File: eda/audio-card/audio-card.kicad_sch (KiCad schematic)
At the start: 1 part, among them J1 AudioJack2_SwitchT

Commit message: Interim commit
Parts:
- removed J1: AudioJack2_SwitchT, Connector_Audio:Jack_3.5mm_PJ320E_Horizontal, symbol Connector_Audio:AudioJack2_SwitchT
- added U1: 74LS74, symbol 74ls593:74LS74
- added U3: 74HCT138, Package_DIP:DIP-16_W10.16mm, symbol 74ls593:74LS138
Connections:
- new net A0: U3.3 (A2)
- new net A1: U3.2 (A1)
- new net A2: U3.1 (A0)
- new net Channel/~{NoteLatch}: U3.14 (O1)
- new net Channel/~{OctaveLatch}: U3.15 (O0)
- new net Channel/~{VolumeLatch}: U3.13 (O2)
- new net Expansion/Clock: U3.6 (E3)
- new net Expansion/R~{W}: U3.4 (E1)
- new net Expansion/~{CS}: U3.5 (E2)
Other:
- added sheet Output stage (output.kicad_sch)
- sheet Channel ports: added D[0..7], MainClock, SoundOut, ~{NoteLatch}, ~{OctaveLatch}, ~{Reset}, ~{VolumeLatch}; removed none
- sheet Expansion ports: added A[0..15], Clock, D[0..7], GND, R~{W}, VCC, ~{CS}, ~{IRQ}, ~{RST}; removed none
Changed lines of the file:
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@@
 (kicad_sch (version 20230121) (generator eeschema)
   (paper "A4")
-  (symbol (lib_id "Connector_Audio:AudioJack2_SwitchT") (at 219.075 62.23 0) (unit 1)
+  (bus_entry (at 64.77 69.215) (size 2.54 2.54)
+    (stroke (width 0) (type default))
+  )
+  (bus_entry (at 64.77 74.295) (size 2.54 2.54)
+    (stroke (width 0) (type default))
+  )
+  (bus_entry (at 64.77 71.755) (size 2.54 2.54)
+    (stroke (width 0) (type default))
+  )
+  (wire (pts (xy 67.31 74.295) (xy 73.025 74.295))
+    (stroke (width 0) (type default))
+  )
+  (bus (pts (xy 111.76 45.085) (xy 76.2 45.085))
+    (stroke (width 0) (type default))
+  )
+  (wire (pts (xy 60.96 84.455) (xy 73.025 84.455))
+    (stroke (width 0) (type default))
+  )
+  (wire (pts (xy 111.76 50.8) (xy 100.965 50.8))
+    (stroke (width 0) (type default))
+  )
+  (bus (pts (xy 60.96 81.915) (xy 64.77 81.915))
+    (stroke (width 0) (type default))
+  )
+  (wire (pts (xy 74.295 50.165) (xy 74.295 42.545))
+    (stroke (width 0) (type default))
+  )
+  (bus (pts (xy 76.2 45.085) (xy 76.2 52.07))
+    (stroke (width 0) (type default))
+  )
+  (wire (pts (xy 104.775 76.835) (xy 98.425 76.835))
+    (stroke (width 0) (type default))
+  )
+  (wire (pts (xy 60.96 86.995) (xy 73.025 86.995))
+    (stroke (width 0) (type default))
+  )
+  (wire (pts (xy 67.31 71.755) (xy 73.025 71.755))
+    (stroke (width 0) (type default))
+  )
+  (wire (pts (xy 60.96 50.165) (xy 74.295 50.165))
+    (stroke (width 0) (type default))
+  )
+  (wire (pts (xy 104.775 54.61) (xy 104.775 76.835))
+    (stroke (width 0) (type default))
+  )
+  (bus (pts (xy 60.96 52.07) (xy 76.2 52.07))
+    (stroke (width 0) (type default))
+  )
+  (bus (pts (xy 64.77 71.755) (xy 64.77 74.295))
+    (stroke (width 0) (type default))
+  )
+  (wire (pts (xy 67.31 76.835) (xy 73.025 76.835))
+    (stroke (width 0) (type default))
+  )
+  (wire (pts (xy 102.87 74.295) (xy 102.87 52.705))
+    (stroke (width 0) (type default))
+  )
+  (wire (pts (xy 102.87 52.705) (xy 111.76 52.705))
+    (stroke (width 0) (type default))
+  )
+  (wire (pts (xy 100.965 50.8) (xy 100.965 71.755))
+    (stroke (width 0) (type default))
+  )
+  (bus (pts (xy 64.77 69.215) (xy 64.77 71.755))
+    (stroke (width 0) (type default))
+  )
+  (wire (pts (xy 60.96 89.535) (xy 73.025 89.535))
+    (stroke (width 0) (type default))
+  )
+  (wire (pts (xy 100.965 71.755) (xy 98.425 71.755))
+    (stroke (width 0) (type default))
+  )
+  (bus (pts (xy 64.77 74.295) (xy 64.77 81.915))
+    (stroke (width 0) (type default))
+  )
+  (wire (pts (xy 98.425 74.295) (xy 102.87 74.295))
+    (stroke (width 0) (type default))
+  )
+  (wire (pts (xy 111.76 54.61) (xy 104.775 54.61))
+    (stroke (width 0) (type default))
+  )
+  (wire (pts (xy 74.295 42.545) (xy 111.76 42.545))
+    (stroke (width 0) (type default))
+  )
+  (label "A2" (at 70.485 71.755 0)
+    (effects (font (size 1.27 1.27)) (justify left bottom))
+  )
+  (label "A0" (at 70.485 76.835 0)
+    (effects (font (size 1.27 1.27)) (justify left bottom))
+  )
+  (label "A1" (at 70.485 74.295 0)
+    (effects (font (size 1.27 1.27)) (justify left bottom))
+  )
+  (symbol (lib_id "74ls593:74LS74") (at 42.545 182.245 0) (unit 3)
     (in_bom yes) (on_board yes) (dnp no) (fields_autoplaced)
-    (property "Reference" "J1" (at 218.44 54.61 0)
-      (effects (font (size 1.27 1.27)))
-    )
-    (property "Value" "AudioJack2_SwitchT" (at 218.44 57.15 0)
-      (effects (font (size 1.27 1.27)))
-    )
-    (property "Footprint" "Connector_Audio:Jack_3.5mm_PJ320E_Horizontal" (at 219.075 62.23 0)
-      (effects (font (size 1.27 1.27)) hide)
-    )
-    (property "Datasheet" "~" (at 219.075 62.23 0)
-      (effects (font (size 1.27 1.27)) hide)
-    )
-    (pin "S")
-    (pin "T")
-    (pin "TN")
+    (property "Reference" "U1" (at 49.53 181.61 0)
+      (effects (font (size 1.27 1.27)) (justify left))
+    )
+    (property "Value" "74LS74" (at 49.53 184.15 0)
+      (effects (font (size 1.27 1.27)) (justify left))
+    )
+    (property "Footprint" "" (at 42.545 182.245 0)
+      (effects (font (size 1.27 1.27)) hide)
+    )
+    (property "Datasheet" "74xx/74hc_hct74.pdf" (at 42.545 182.245 0)
+      (effects (font (size 1.27 1.27)) hide)
+    )
+    (pin "1")
+    (pin "2")
+    (pin "3")
+    (pin "4")
+    (pin "5")
+    (pin "6")
+    (pin "10")
+    (pin "11")
+    (pin "12")
+    (pin "13")
+    (pin "8")
+    (pin "9")
+    (pin "14")
+    (pin "7")
     (instances
       (project "audio-card"
         (path "/b2d5e230-38ae-42d2-af04-44d0ea9b43d4"
-          (reference "J1") (unit 1)
+          (reference "U1") (unit 3)
+        )
+      )
+    )
+  )
+  (symbol (lib_id "74ls593:74LS138") (at 85.725 79.375 0) (unit 1)
+    (in_bom yes) (on_board yes) (dnp no) (fields_autoplaced)
+    (property "Reference" "U3" (at 87.6809 65.405 0)
+      (effects (font (size 1.27 1.27)) (justify left))
+    )
+    (property "Value" "74HCT138" (at 87.6809 67.945 0)
+      (effects (font (size 1.27 1.27)) (justify left))
+    )
+    (property "Footprint" "Package_DIP:DIP-16_W10.16mm" (at 85.725 79.375 0)
+      (effects (font (size 1.27 1.27)) hide)
+    )
+    (property "Datasheet" "http://www.ti.com/lit/gpn/sn74LS138" (at 85.725 79.375 0)
+      (effects (font (size 1.27 1.27)) hide)
+    )
+    (pin "1")
+    (pin "10")
+    (pin "11")
+    (pin "12")
+    (pin "13")
+    (pin "14")
+    (pin "15")
+    (pin "16")
+    (pin "2")
+    (pin "3")
+    (pin "4")
+    (pin "5")
+    (pin "6")
+    (pin "7")
+    (pin "8")
+    (pin "9")
+    (instances
+      (project "audio-card"
+        (path "/b2d5e230-38ae-42d2-af04-44d0ea9b43d4"
+          (reference "U3") (unit 1)
         )
       )
@@
       (effects (font (size 1.27 1.27)) (justify left top))
     )
+    (pin "D[0..7]" tri_state (at 60.96 52.07 0)
+      (effects (font (size 1.27 1.27)) (justify right))
+    )
+    (pin "GND" output (at 46.355 90.17 180)
+      (effects (font (size 1.27 1.27)) (justify left))
+    )
+    (pin "R~{W}" output (at 60.96 89.535 0)
+      (effects (font (size 1.27 1.27)) (justify right))
+    )
+    (pin "Clock" output (at 60.96 84.455 0)
+      (effects (font (size 1.27 1.27)) (justify right))
+    )
+    (pin "~{CS}" output (at 60.96 86.995 0)
+      (effects (font (size 1.27 1.27)) (justify right))
+    )
+    (pin "~{IRQ}" output (at 60.96 60.96 0)
+      (effects (font (size 1.27 1.27)) (justify right))
+    )
+    (pin "~{RST}" bidirectional (at 60.96 50.165 0)
+      (effects (font (size 1.27 1.27)) (justify right))
+    )
+    (pin "VCC" output (at 46.355 48.895 180)
+      (effects (font (size 1.27 1.27)) (justify left))
+    )
+    (pin "A[0..15]" output (at 60.96 81.915 0)
+      (effects (font (size 1.27 1.27)) (justify right))
+    )
     (instances
       (project "audio-card"
@@
     )
   )
-  (sheet (at 113.03 34.29) (size 16.51 25.4) (fields_autoplaced)
+  (sheet (at 173.99 83.82) (size 12.7 3.81) (fields_autoplaced)
     (stroke (width 0.1524) (type solid))
     (fill (color 0 0 0 0.0000))
-    (property "Sheetname" "Channel" (at 113.03 33.5784 0)
+    (property "Sheetname" "Output stage" (at 173.99 83.1084 0)
       (effects (font (size 1.27 1.27)) (justify left bottom))
     )
-    (property "Sheetfile" "channel.kicad_sch" (at 113.03 60.2746 0)
+    (property "Sheetfile" "output.kicad_sch" (at 173.99 88.2146 0)
       (effects (font (size 1.27 1.27)) (justify left top))
     )
-    (instances
+    (pin "SoundIn" input (at 173.99 85.725 180)
+      (effects (font (size 1.27 1.27)) (justify left))
+    )
+    (instances
+      (project "audio-card"
+        (path "/b2d5e230-38ae-42d2-af04-44d0ea9b43d4" (page "4"))
+      )
+    )
+  )
+  (sheet (at 111.76 37.465) (size 16.51 25.4) (fields_autoplaced)
+    (stroke (width 0.1524) (type solid))
+    (fill (color 0 0 0 0.0000))
+    (property "Sheetname" "Channel" (at 111.76 36.7534 0)
+      (effects (font (size 1.27 1.27)) (justify left bottom))
+    )
+    (property "Sheetfile" "channel.kicad_sch" (at 111.76 63.4496 0)
+      (effects (font (size 1.27 1.27)) (justify left top))
+    )
+    (pin "~{Reset}" input (at 111.76 42.545 180)
+      (effects (font (size 1.27 1.27)) (justify left))
+    )
+    (pin "~{NoteLatch}" input (at 111.76 52.705 180)
+      (effects (font (size 1.27 1.27)) (justify left))
+    )
+    (pin "MainClock" input (at 111.76 39.37 180)
+      (effects (font (size 1.27 1.27)) (justify left))
+    )
+    (pin "SoundOut" output (at 128.27 60.325 0)
+      (effects (font (size 1.27 1.27)) (justify right))
+    )
+    (pin "D[0..7]" input (at 111.76 45.085 180)
+      (effects (font (size 1.27 1.27)) (justify left))
+    )
+    (pin "~{OctaveLatch}" input (at 111.76 50.8 180)
+      (effects (font (size 1.27 1.27)) (justify left))
+    )
+    (pin "~{VolumeLatch}" input (at 111.76 54.61 180)
+      (effects (font (size 1.27 1.27)) (justify left))
+    )
+    (instances

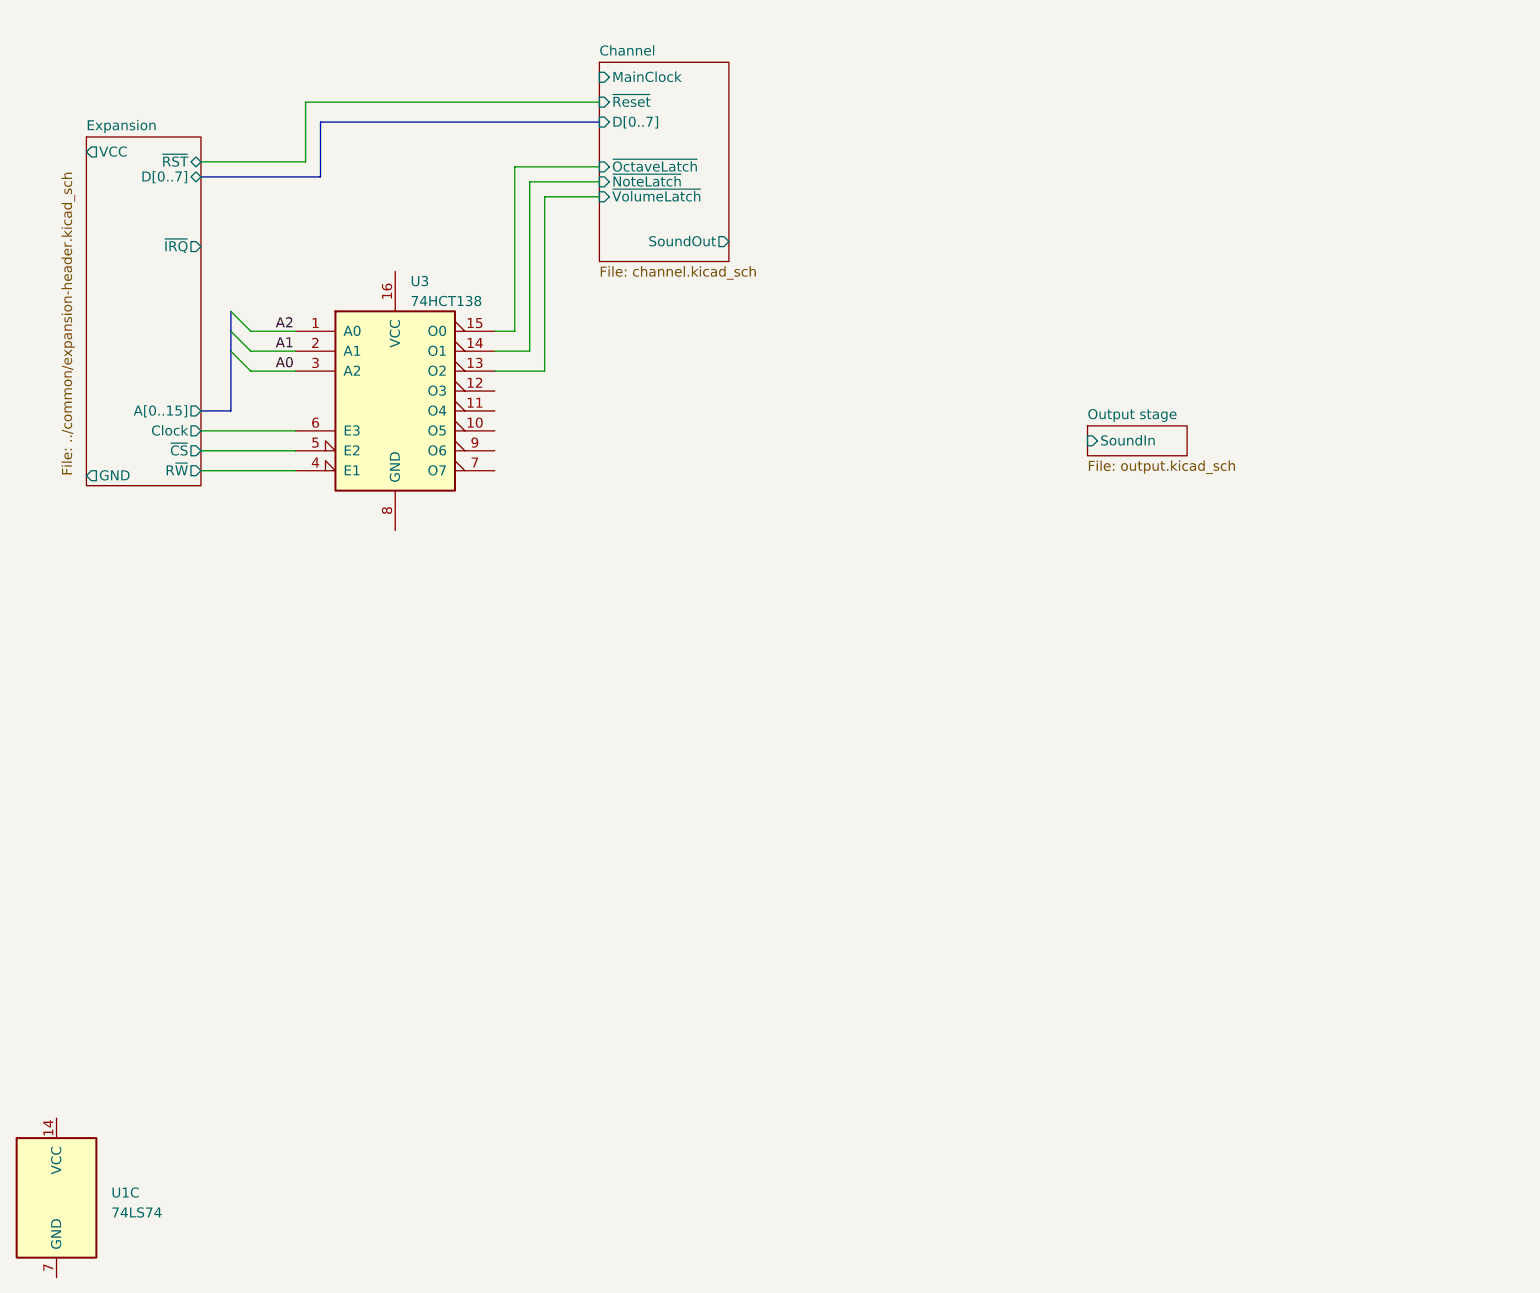
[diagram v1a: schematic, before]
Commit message: Start converting audio card to analog synth base
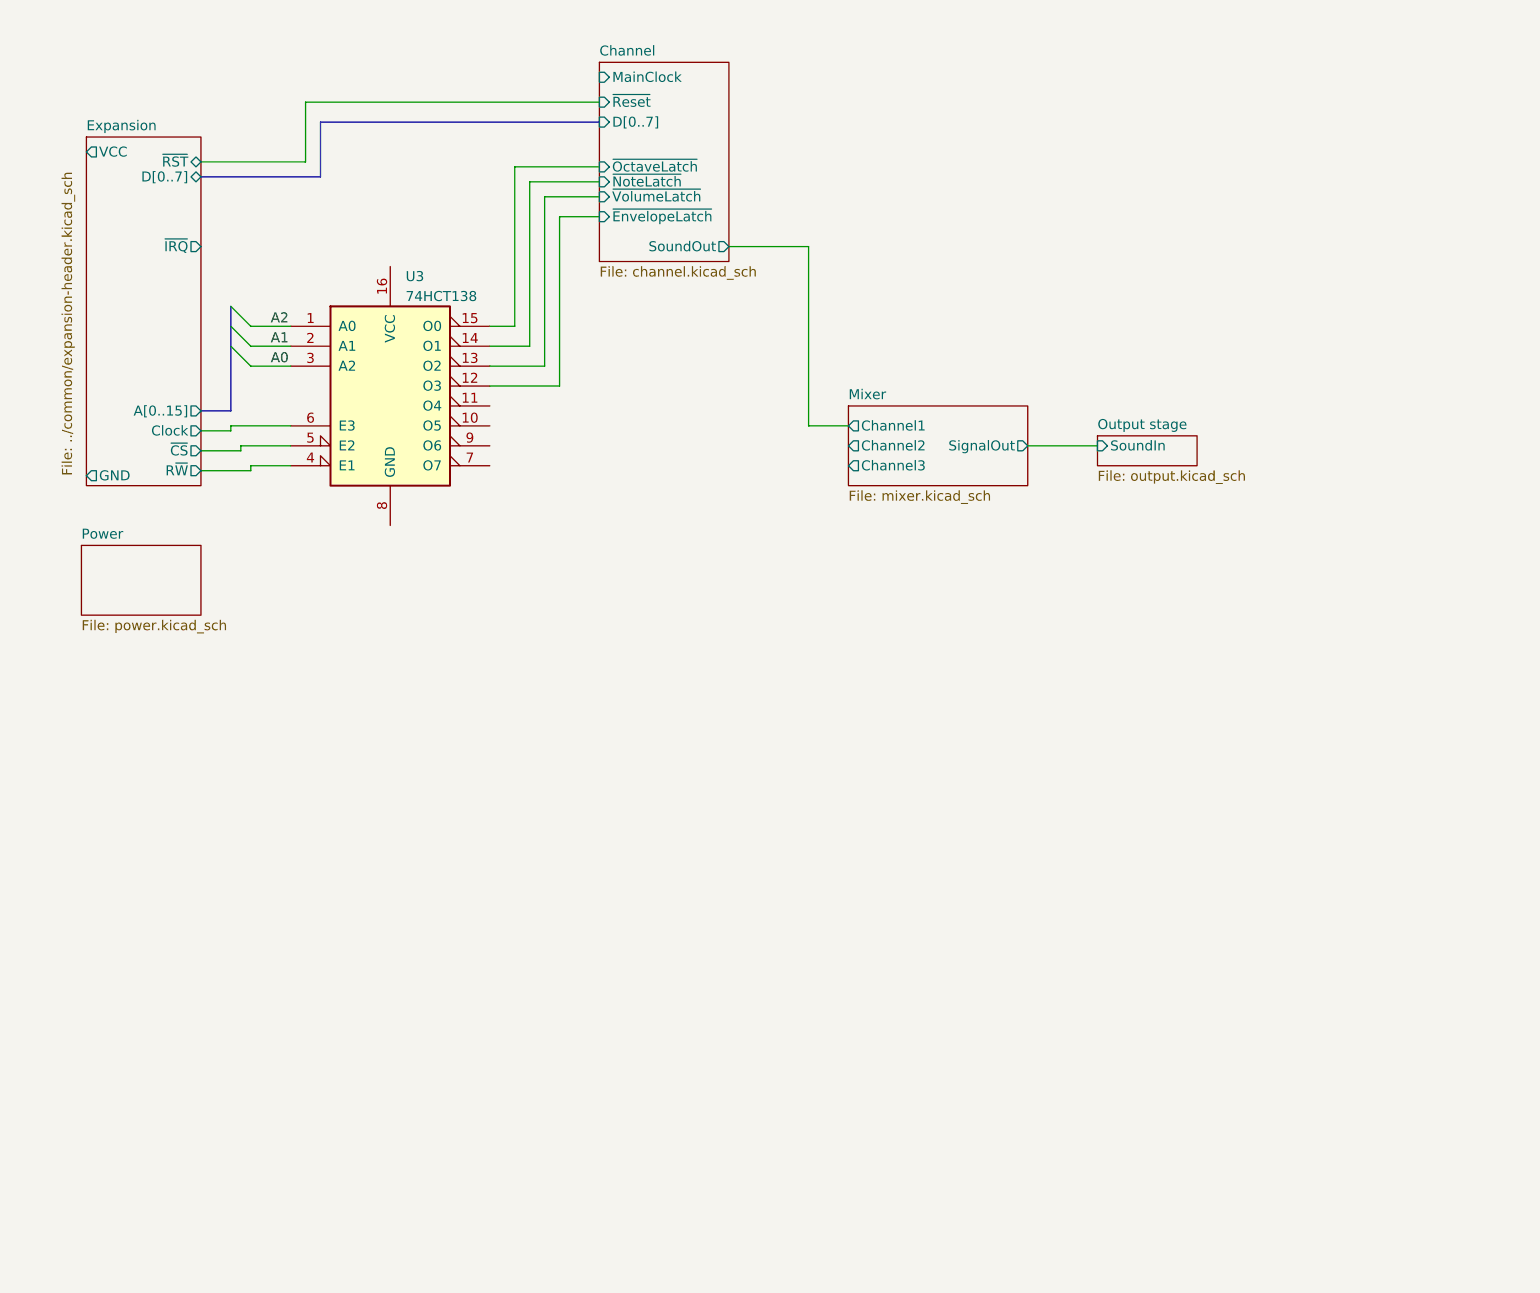
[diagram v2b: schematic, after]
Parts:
- removed U1: 74LS74, symbol 74ls593:74LS74
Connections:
- net Channel/~{EnvelopeLatch}: now reaches U3.12 (O3)
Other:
- added sheet Mixer (mixer.kicad_sch)
- added sheet Power (power.kicad_sch)
- sheet Channel ports: added ~{EnvelopeLatch}; removed none
- moved on the sheet: U3
